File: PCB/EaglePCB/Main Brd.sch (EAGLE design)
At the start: 58 parts, among them J1 1909763-1, J2 702461401, J3 1909763-1, U1 ATWINC1500-MR210PB1952-T, U3 MSP430FR2355TDBTRDBT0038A_M, U6 ARJM11C7-114-BA-EW2

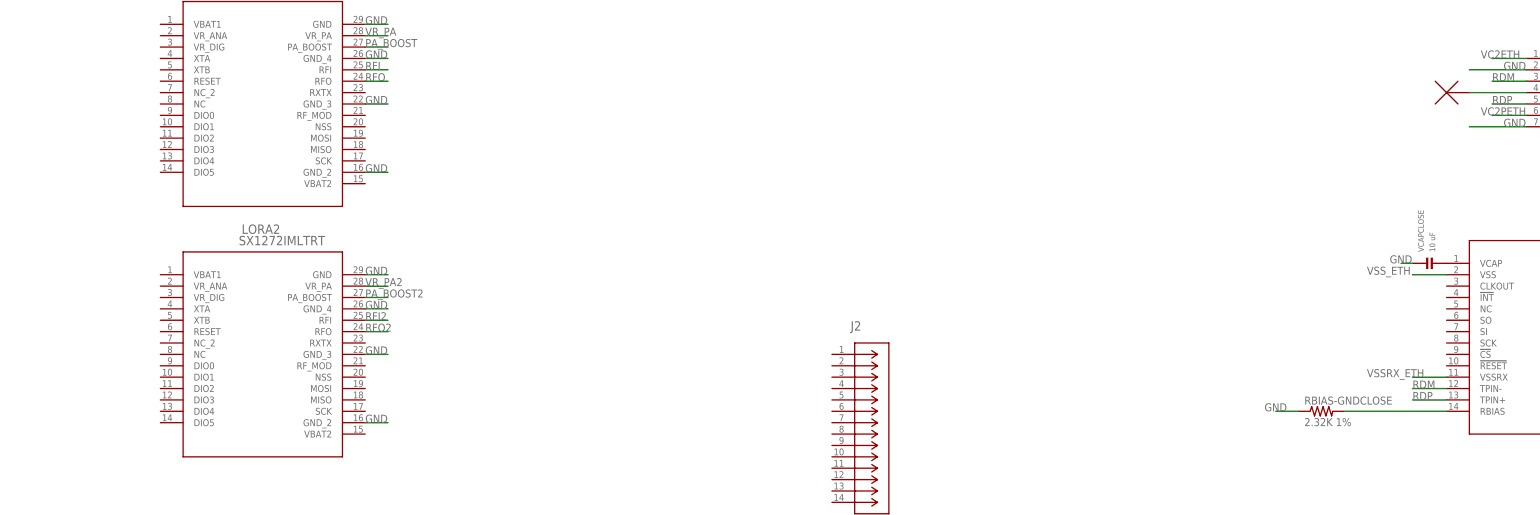
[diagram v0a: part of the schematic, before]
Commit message: added wire labels
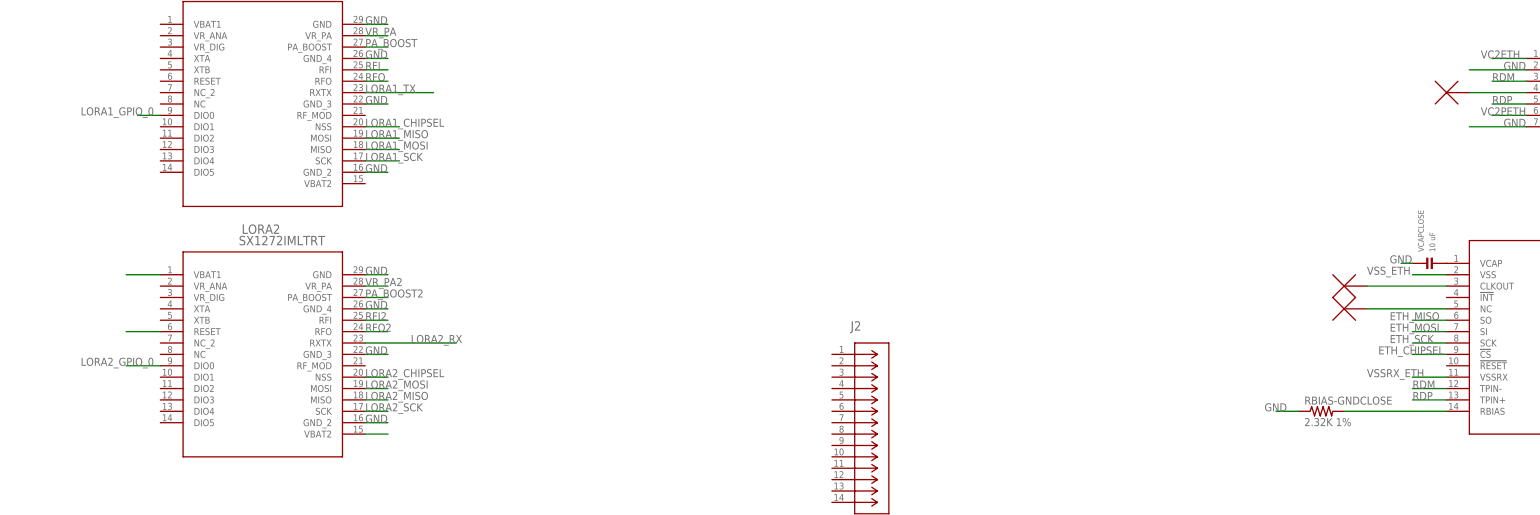
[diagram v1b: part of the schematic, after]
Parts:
- added U$3, U$4: NC_MARKER, NC_MARKER:NC_MARKER
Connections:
- new net ETH_CHIPSEL: ETH.!CS
- new net ETH_MISO: ETH.SO
- new net ETH_MOSI: ETH.SI
- new net ETH_SCK: ETH.SCK
- new net LORA1_CHIPSEL: LORA1.NSS
- new net LORA1_GPIO_0: LORA1.DIO0
- new net LORA1_MISO: LORA1.MOSI
- new net LORA1_MOSI: LORA1.MISO
- new net LORA1_SCK: LORA1.SCK
- new net LORA1_TX: LORA1.RXTX
- new net LORA2_CHIPSEL: LORA2.NSS
- new net LORA2_GPIO_0: LORA2.DIO0
- new net LORA2_MISO: LORA2.MISO
- new net LORA2_MOSI: LORA2.MOSI
- new net LORA2_RX: LORA2.RXTX
- new net LORA2_SCK: LORA2.SCK
- new net N$11: LORA2.RESET
- new net N$12: LORA2.VBAT2
- new net N$13: LORA2.VBAT1
- new net N$14: ETH.NC, U$3.P$1
- new net N$15: ETH.CLKOUT, U$4.P$1
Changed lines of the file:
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@@
 <layers>
 <layer number="1" name="Top" color="4" fill="1" visible="no" active="no"/>
+<layer number="2" name="Route2" color="16" fill="1" visible="no" active="no"/>
+<layer number="3" name="Route3" color="17" fill="1" visible="no" active="no"/>
+<layer number="4" name="Route4" color="18" fill="1" visible="no" active="no"/>
+<layer number="5" name="Route5" color="19" fill="1" visible="no" active="no"/>
+<layer number="6" name="Route6" color="25" fill="1" visible="no" active="no"/>
+<layer number="7" name="Route7" color="26" fill="1" visible="no" active="no"/>
+<layer number="8" name="Route8" color="27" fill="1" visible="no" active="no"/>
+<layer number="9" name="Route9" color="28" fill="1" visible="no" active="no"/>
+<layer number="10" name="Route10" color="29" fill="1" visible="no" active="no"/>
+<layer number="11" name="Route11" color="30" fill="1" visible="no" active="no"/>
+<layer number="12" name="Route12" color="20" fill="1" visible="no" active="no"/>
+<layer number="13" name="Route13" color="21" fill="1" visible="no" active="no"/>
+<layer number="14" name="Route14" color="22" fill="1" visible="no" active="no"/>
+<layer number="15" name="Route15" color="23" fill="1" visible="no" active="no"/>
 <layer number="16" name="Bottom" color="1" fill="1" visible="no" active="no"/>
 <layer number="17" name="Pads" color="2" fill="1" visible="no" active="no"/>
@@
 <part name="U$2" library="473" deviceset="J49SMH-P-G-G-K-25M0" device=""/>
 <part name="J2" library="473" deviceset="702461401" device=""/>
+<part name="U$3" library="NC_MARKER" deviceset="NC_MARKER" device=""/>
+<part name="U$4" library="NC_MARKER" deviceset="NC_MARKER" device=""/>
 </parts>
 <sheets>
@@
 <attribute name="NAME" x="80.3656" y="33.2486" size="2.0828" layer="95" ratio="6" rot="SR0"/>
 </instance>
+<instance part="U$3" gate="G$1" x="190.5" y="38.1" smashed="yes"/>
+<instance part="U$4" gate="G$1" x="190.5" y="43.18" smashed="yes"/>
 </instances>
 <busses>
@@
 </segment>
 </net>
+<net name="N$11" class="0">
+<segment>
+<pinref part="LORA2" gate="A" pin="RESET"/>
+<wire x1="-73.66" y1="33.02" x2="-81.28" y2="33.02" width="0.1524" layer="91"/>
+</segment>
+</net>
+<net name="N$12" class="0">
+<segment>
+<pinref part="LORA2" gate="A" pin="VBAT2"/>
+<wire x1="-27.94" y1="10.16" x2="-22.86" y2="10.16" width="0.1524" layer="91"/>
+</segment>
+</net>
+<net name="N$13" class="0">
+<segment>
+<pinref part="LORA2" gate="A" pin="VBAT1"/>
+<wire x1="-73.66" y1="45.72" x2="-81.28" y2="45.72" width="0.1524" layer="91"/>
+</segment>
+</net>
+<net name="LORA2_GPIO_0" class="0">
+<segment>
+<pinref part="LORA2" gate="A" pin="DIO0"/>
+<wire x1="-73.66" y1="25.4" x2="-81.28" y2="25.4" width="0.1524" layer="91"/>
+<label x="-91.44" y="25.4" size="1.778" layer="95"/>
+</segment>
+</net>
+<net name="LORA2_MOSI" class="0">
+<segment>
+<pinref part="LORA2" gate="A" pin="MOSI"/>
+<wire x1="-27.94" y1="20.32" x2="-22.86" y2="20.32" width="0.1524" layer="91"/>
+<label x="-27.94" y="20.32" size="1.778" layer="95"/>
+</segment>
+</net>
+<net name="LORA2_MISO" class="0">
+<segment>
+<pinref part="LORA2" gate="A" pin="MISO"/>
+<wire x1="-27.94" y1="17.78" x2="-22.86" y2="17.78" width="0.1524" layer="91"/>
+<label x="-27.94" y="17.78" size="1.778" layer="95"/>
+</segment>
+</net>
+<net name="LORA2_SCK" class="0">
+<segment>
+<pinref part="LORA2" gate="A" pin="SCK"/>
+<wire x1="-27.94" y1="15.24" x2="-22.86" y2="15.24" width="0.1524" layer="91"/>
+<label x="-27.94" y="15.24" size="1.778" layer="95"/>
+</segment>
+</net>
+<net name="LORA2_CHIPSEL" class="0">
+<segment>
+<pinref part="LORA2" gate="A" pin="NSS"/>
+<wire x1="-27.94" y1="22.86" x2="-22.86" y2="22.86" width="0.1524" layer="91"/>
+<label x="-27.94" y="22.86" size="1.778" layer="95"/>
+</segment>
+</net>
+<net name="LORA2_RX" class="0">
+<segment>
+<pinref part="LORA2" gate="A" pin="RXTX"/>
+<wire x1="-27.94" y1="30.48" x2="-7.62" y2="30.48" width="0.1524" layer="91"/>
+<label x="-17.78" y="30.48" size="1.778" layer="95"/>
+</segment>
+</net>
+<net name="LORA1_TX" class="0">
+<segment>
+<pinref part="LORA1" gate="A" pin="RXTX"/>
+<wire x1="-27.94" y1="86.36" x2="-12.7" y2="86.36" width="0.1524" layer="91"/>
+<label x="-27.94" y="86.36" size="1.778" layer="95"/>
+</segment>
+</net>
+<net name="LORA1_CHIPSEL" class="0">
+<segment>
+<pinref part="LORA1" gate="A" pin="NSS"/>
+<wire x1="-27.94" y1="78.74" x2="-20.32" y2="78.74" width="0.1524" layer="91"/>
+<label x="-27.94" y="78.74" size="1.778" layer="95"/>
+</segment>
+</net>
+<net name="LORA1_MISO" class="0">
+<segment>
+<pinref part="LORA1" gate="A" pin="MOSI"/>
+<wire x1="-27.94" y1="76.2" x2="-20.32" y2="76.2" width="0.1524" layer="91"/>
+<label x="-27.94" y="76.2" size="1.778" layer="95"/>
+</segment>
+</net>
+<net name="LORA1_MOSI" class="0">
+<segment>
+<pinref part="LORA1" gate="A" pin="MISO"/>
+<wire x1="-27.94" y1="73.66" x2="-20.32" y2="73.66" width="0.1524" layer="91"/>
+<label x="-27.94" y="73.66" size="1.778" layer="95"/>
+</segment>
+</net>
+<net name="LORA1_SCK" class="0">
+<segment>
+<pinref part="LORA1" gate="A" pin="SCK"/>
+<wire x1="-27.94" y1="71.12" x2="-20.32" y2="71.12" width="0.1524" layer="91"/>
+<label x="-27.94" y="71.12" size="1.778" layer="95"/>
+</segment>
+</net>
+<net name="LORA1_GPIO_0" class="0">
+<segment>
+<pinref part="LORA1" gate="A" pin="DIO0"/>
+<wire x1="-73.66" y1="81.28" x2="-78.74" y2="81.28" width="0.1524" layer="91"/>
+<label x="-91.44" y="81.28" size="1.778" layer="95"/>
+</segment>
+</net>
+<net name="ETH_CHIPSEL" class="0">
+<segment>
+<pinref part="ETH" gate="A" pin="!CS"/>
+<wire x1="213.36" y1="27.94" x2="205.74" y2="27.94" width="0.1524" layer="91"/>
+<label x="198.12" y="27.94" size="1.778" layer="95"/>
+</segment>
+</net>
+<net name="ETH_SCK" class="0">
+<segment>
+<pinref part="ETH" gate="A" pin="SCK"/>
+<wire x1="213.36" y1="30.48" x2="205.74" y2="30.48" width="0.1524" layer="91"/>
+<label x="200.66" y="30.48" size="1.778" layer="95"/>
+</segment>
+</net>
+<net name="ETH_MOSI" class="0">
+<segment>
+<pinref part="ETH" gate="A" pin="SI"/>
+<wire x1="213.36" y1="33.02" x2="205.74" y2="33.02" width="0.1524" layer="91"/>
+<label x="200.66" y="33.02" size="1.778" layer="95"/>
+</segment>
+</net>
+<net name="ETH_MISO" class="0">
+<segment>
+<pinref part="ETH" gate="A" pin="SO"/>
+<wire x1="213.36" y1="35.56" x2="205.74" y2="35.56" width="0.1524" layer="91"/>
+<label x="200.66" y="35.56" size="1.778" layer="95"/>
+</segment>
+</net>
+<net name="N$14" class="0">
+<segment>
+<pinref part="ETH" gate="A" pin="NC"/>
+<wire x1="213.36" y1="38.1" x2="195.58" y2="38.1" width="0.1524" layer="91"/>
+<pinref part="U$3" gate="G$1" pin="P$1"/>
+</segment>
+</net>
+<net name="N$15" class="0">
+<segment>
+<pinref part="ETH" gate="A" pin="CLKOUT"/>
+<wire x1="213.36" y1="43.18" x2="195.58" y2="43.18" width="0.1524" layer="91"/>
+<pinref part="U$4" gate="G$1" pin="P$1"/>
+</segment>
+</net>

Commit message: All Passives Complete
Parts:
- added !MSP_RST!_3V3: 47 kOhm, Resistor_Capacitor:RC0603JR-070RL
- added R2: RC0603JR-070RL, Resistor_Capacitor:RC0603JR-070RL
- added R3: 10 uF, microbuilder:RESISTOR2012
- added RD-GND2, RD-GND3, RD-GND4: 0.1 uF, microbuilder:CAP_CERAMIC0603
- added TCXO1, TCXO2: TCXO_32,000MHZ, 473:TCXO_32,000MHZ
- added U$5, U$6: NC_MARKER, NC_MARKER:NC_MARKER
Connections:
- net ETH_CHIPSEL renamed !ETH_CHIPSEL
- net LORA1_GPIO_0 renamed LORA1_IRQ
- net LORA2_GPIO_0 renamed LORA2_IRQ
- net N$11 renamed LORA2_RST
- net N$3 renamed NC_1
- net RDM renamed RD_N
- net RDP renamed RD_P
- net TDC renamed TD_C
- net TDM renamed TD_N
- net TDP renamed TD_P
- removed net VDDOSC_ETH: ETH.VDDOSC, VSSOSC-VDDOSC.P$1
- removed net VDDPLL_ETH: ETH.VDDPLL, VSSPLL-VDDPLL.P$1
- removed net VDDRX_ETH: ETH.VDDRX, VSSRX-VDDRX.P$2
- removed net VDDTX_ETH: ETH.VDDTX, VSSTX-VDDTX.P$2
- removed net VDD_ETH: ETH.VDD, VSS-VDD_ETH.P$2
- removed net VSSOSC_ETH: ETH.VSSOSC, VSSOSC-VDDOSC.P$2
- removed net VSSPLL_ETH: ETH.VSSPLL, VSSPLL-VDDPLL.P$2
- removed net VSSRX_ETH: ETH.VSSRX, VSSRX-VDDRX.P$1
- removed net VSSTX_ETH: ETH.VSSTX, VSSTX-VDDTX.P$1
- removed net VSS_ETH: ETH.VSS, VSS-VDD_ETH.P$1
- new net !ATC_IRQ: U1.IRQN
- new net !ATC_RST: U1.RESET_N
- new net !ETH_IRQ: ETH.!INT
- new net !ETH_RST: ETH.!RESET
- new net !MSP_RST: !MSP_RST!_3V3.1, J2.11, U3.RST_NMI_SBWTDIO_N
- new net A0_CLK: J2.5, U3.P1.5_UCA0CLK_TMS_OA1O_A5
- new net A0_MISO: J2.3, U3.P1.6_UCA0RXD_UCA0SOMI_TB0.1_TDI_TCLK_OA1-_A6
- new net A0_MOSI: J2.1, U3.P1.7_UCA0TXD_UCA0SIMO_TB0.2_TDO_OA1+_A7_VREF+
- new net A1_CLK: U3.P4.1_UCA1CLK
- new net A1_MISO: U3.P4.2_UCA1RXD_UCA1SOMI_UCA1RXD_N
- new net A1_MOSI: U3.P4.3_UCA1TXD_UCA1SIMO_UCA1TXD_N
- new net ATC_EN: U1.CHIP_EN
- new net ATC_MISO: U1.SPI_MISO
- new net ATC_MOSI: U1.SPI_MOSI
- new net ATC_SPI_CFG: R2.2, U1.SPI_CFG
- new net ATC_SSN: U1.SPI_SSN
- new net B0_CLK: U3.P1.1_UCB0CLK_ACLK_OA0O_COMP0.1_A1
- new net B0_MISO: U3.P1.2_UCB0SIMO_UCB0SDA_TB0TRG_OA0-_A2_VEREF-
- new net B0_MOSI: U3.P1.3_UCB0SOMI_OA0+_A3
- new net B1_CLK: U3.P4.5_UCB1CLK
- new net B1_MISO: U3.P4.6_UCB1SIMO_UCB1SDA
- new net B1_MOSI: U3.P4.7_UCB1SOMI_UCB1SCL
- new net LORA1_RST: LORA1.RESET
- new net MSP_TCK: J2.7, U3.P1.4_UCA0STE_TCK_A4
- new net MSP_TEST: J2.8, U3.TEST_SBWTCK
- new net MSP_VCC: J2.2
- new net MSP_VCC_TAR: J2.4
- new net N$21: U3.P4.0_UCA1STE_ISOTXD_ISORXD
- new net N$3: LORA1.RF_MOD, U$6.P$1
- new net SPI_SCK: U1.SPI_SCK
- new net XTA1: LORA1.XTA, TCXO1.OSC
- new net XTA2: LORA2.XTA, TCXO2.OSC
- net 3V3: now also !MSP_RST!_3V3.2, ETH.VDD, ETH.VDDOSC, ETH.VDDPLL, ETH.VDDRX, ETH.VDDTX, LORA1.VBAT1, LORA1.VBAT2, LORA2.VBAT1, LORA2.VBAT2, R2.1, RD-GND2.P$1, RD-GND3.P$1, TCXO1.VCC, TCXO2.VCC, U1.VDDIO, U3.DVCC, VSS-VDD_ETH.P$2, VSSOSC-VDDOSC.P$1, VSSPLL-VDDPLL.P$1, VSSRX-VDDRX.P$2, VSSTX-VDDTX.P$2
- net GND: now also ETH.VSS, ETH.VSSOSC, ETH.VSSPLL, ETH.VSSRX, ETH.VSSTX, J2.9, LORA1.NC, LORA1.NC_2, LORA2.NC, LORA2.NC_2, R3.2, RD-GND2.P$2, RD-GND3.P$2, RD-GND4.P$1, TCXO1.GND, TCXO2.GND, U1.GND_1, U1.GND_2, U1.GND_3, U1.GND_PADDLE, U3.DVSS, VSS-VDD_ETH.P$1, VSSOSC-VDDOSC.P$2, VSSPLL-VDDPLL.P$2, VSSRX-VDDRX.P$1, VSSTX-VDDTX.P$1
- net N$12: now also LORA2.RF_MOD, U$5.P$1; no longer LORA2.VBAT2
- net N$13: now also R3.1, RD-GND4.P$2, U1.1P3V_TP; no longer LORA2.VBAT1
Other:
- note added: "MSP_VCC"
- note added: "MSP_VCC_TAR"
- note added: "TCK"
- note added: "TDI"
- note added: "TDO"
- note added: "TMS"

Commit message: New antenna connector, routing SPI lines
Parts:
- removed J1, J3: 1909763-1, 473:1909763-1
- added X1, X2: (no value), adafruit:SMACONNECTOR_EDGE
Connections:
- removed net ANT3: ANT2-ANT3.1, ANT2-GND1.P$2, J1.SIG
- removed net ANT3-2: ANT2-ANT1.1, ANT2-GND3.P$2, J3.SIG
- new net N$11: ANT2-ANT3.1, ANT2-GND1.P$2, X1.ANT
- new net N$18: ANT2-ANT1.1, ANT2-GND3.P$2, X2.ANT
- net A0_CLK: no longer U3.P1.5_UCA0CLK_TMS_OA1O_A5
- net A0_MISO: no longer U3.P1.6_UCA0RXD_UCA0SOMI_TB0.1_TDI_TCLK_OA1-_A6
- net A0_MOSI: no longer U3.P1.7_UCA0TXD_UCA0SIMO_TB0.2_TDO_OA1+_A7_VREF+
- net ETH_MISO: now also U3.P1.6_UCA0RXD_UCA0SOMI_TB0.1_TDI_TCLK_OA1-_A6
- net ETH_MOSI: now also U3.P1.7_UCA0TXD_UCA0SIMO_TB0.2_TDO_OA1+_A7_VREF+
- net ETH_SCK: now also U3.P1.5_UCA0CLK_TMS_OA1O_A5
- net GND: now also X1.GND1, X1.GND2, X1.GND3, X1.GND4, X2.GND1, X2.GND2, X2.GND3, X2.GND4; no longer J1.GND, J1.GND_2, J3.GND, J3.GND_2

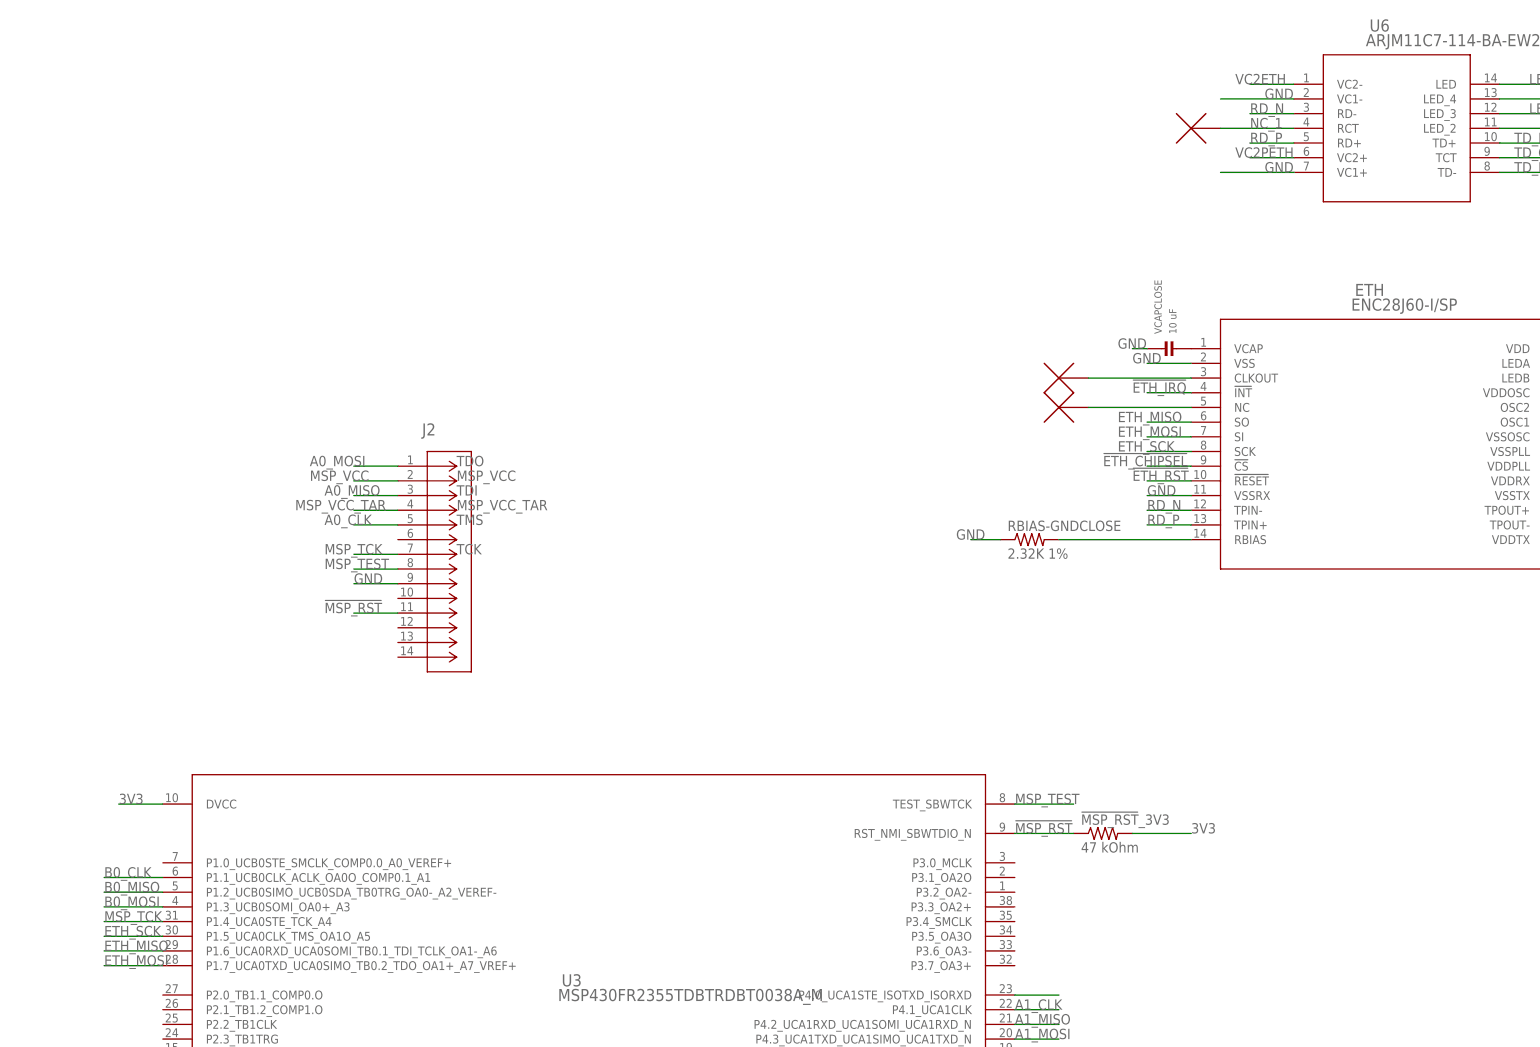
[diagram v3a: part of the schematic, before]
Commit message: more traces ran, ENC, JTAG
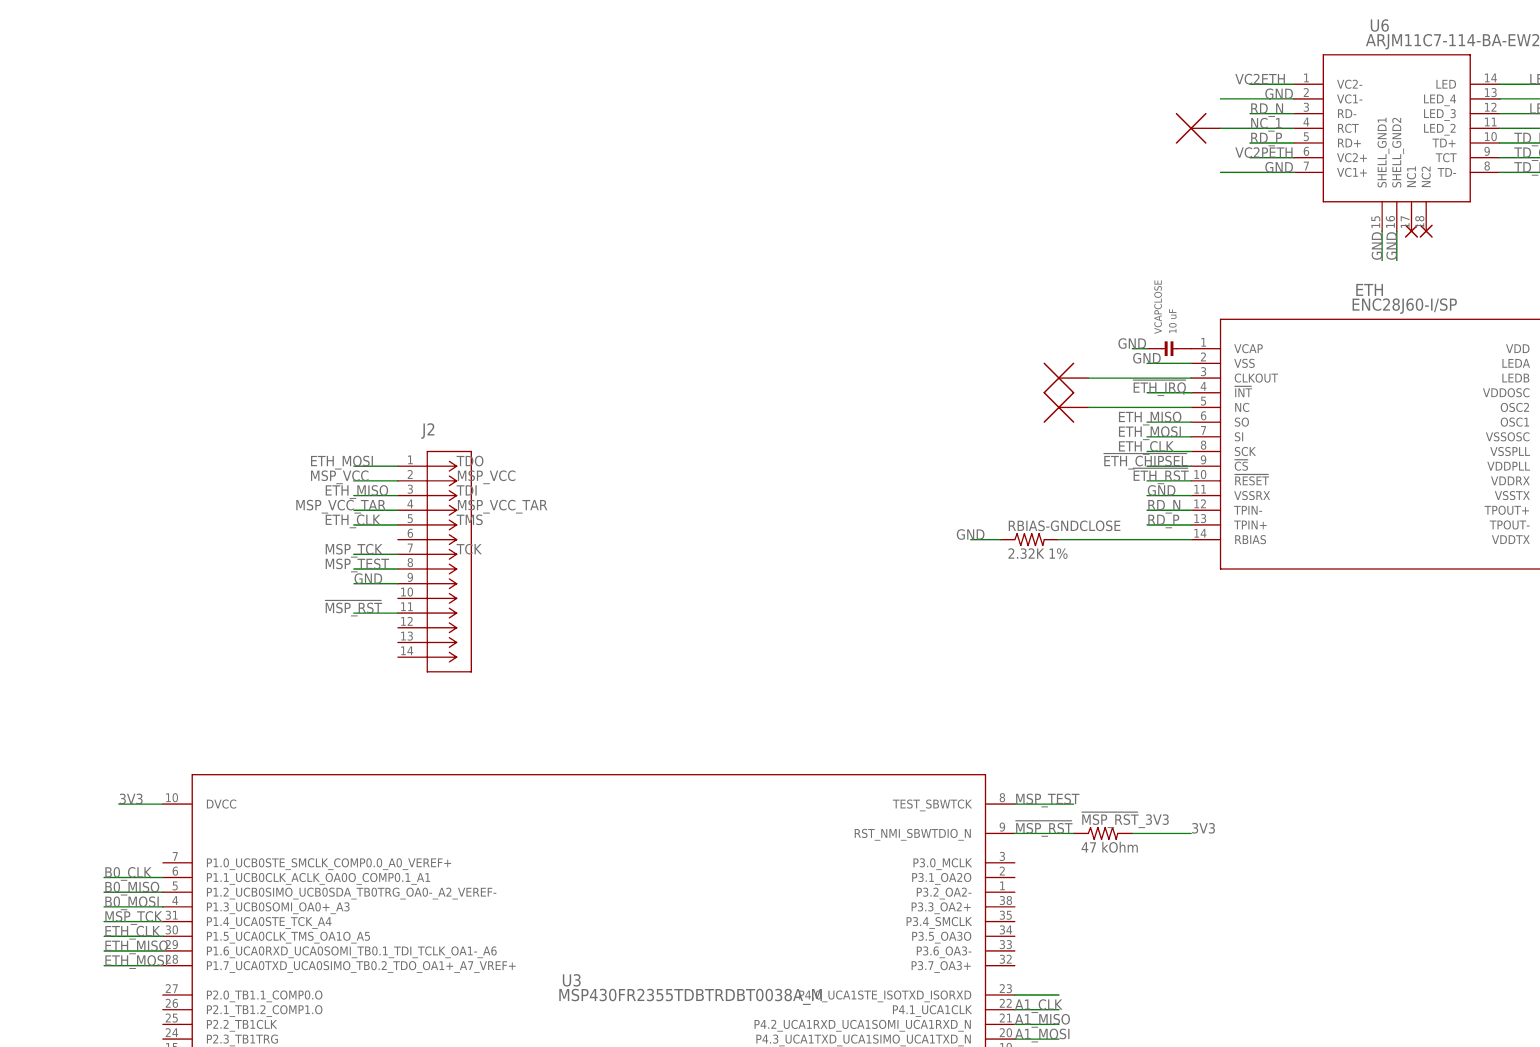
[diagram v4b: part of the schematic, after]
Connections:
- removed net A0_CLK: J2.5
- removed net A0_MISO: J2.3
- removed net A0_MOSI: J2.1
- removed net ETH_SCK: ETH.SCK, U3.P1.5_UCA0CLK_TMS_OA1O_A5
- new net ETH_CLK: ETH.SCK, J2.5, U3.P1.5_UCA0CLK_TMS_OA1O_A5
- net ETH_MISO: now also J2.3
- net ETH_MOSI: now also J2.1
- net GND: now also U6.SHELL_GND1, U6.SHELL_GND2
